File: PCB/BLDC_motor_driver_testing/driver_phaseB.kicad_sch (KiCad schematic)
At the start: 20 parts, among them Q3 IRF540N, Q4 IRF540N, U5 IR2104, U6 INA240A2D, U7 LMV393

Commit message: PCB layouting...
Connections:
- net PWR_12V: now also Q3.2 (D)
- net at C12.1, D5.1 (K), U5.8 (VB): no longer Q3.2 (D)
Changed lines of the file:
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@@
+	)
+	(junction
+		(at 66.04 93.98)
+		(diameter 0)
+		(color 0 0 0 0)
 	)
 	(junction
@@
 	)
 	(junction
+		(at 86.36 35.56)
+		(diameter 0)
+		(color 0 0 0 0)
+	)
+	(junction
 		(at 146.05 127)
 		(diameter 0)
@@
 	)
 	(junction
-		(at 83.82 64.77)
-		(diameter 0)
-		(color 0 0 0 0)
-	)
-	(junction
 		(at 129.54 120.65)
 		(diameter 0)
@@
 	(wire
 		(pts
-			(xy 113.03 64.77) (xy 113.03 69.85)
+			(xy 113.03 35.56) (xy 113.03 69.85)
 		)
 		(stroke
@@
 	(wire
 		(pts
-			(xy 66.04 92.71) (xy 66.04 96.52)
+			(xy 66.04 92.71) (xy 66.04 93.98)
 		)
 		(stroke
@@
 	(wire
 		(pts
+			(xy 55.88 93.98) (xy 66.04 93.98)
+		)
+		(stroke
+			(width 0)
+			(type default)
+		)
+	)
+	(wire
+		(pts
 			(xy 146.05 127) (xy 148.59 127)
 		)
@@
 	(wire
 		(pts
+			(xy 113.03 35.56) (xy 86.36 35.56)
+		)
+		(stroke
+			(width 0)
+			(type default)
+		)
+	)
+	(wire
+		(pts
 			(xy 99.06 74.93) (xy 101.6 74.93)
 		)
@@
 	(wire
 		(pts
-			(xy 83.82 64.77) (xy 113.03 64.77)
-		)
-		(stroke
-			(width 0)
-			(type default)
-		)
-	)
-	(wire
-		(pts
 			(xy 80.01 48.26) (xy 73.66 48.26)
 		)
@@
 		(pts
 			(xy 43.18 80.01) (xy 58.42 80.01)
+		)
+		(stroke
+			(width 0)
+			(type default)
+		)
+	)
+	(wire
+		(pts
+			(xy 66.04 93.98) (xy 66.04 96.52)
 		)
 		(stroke
@@
 		(effects
 			(font
+				(size 1.27 1.27)
+			)
+			(justify right)
+		)
+	)
+	(hierarchical_label "GND"
+		(shape input)
+		(at 55.88 93.98 180)
+		(effects
+			(font

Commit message: Test driver layout...
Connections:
- net GND_B: now reaches C14.1, Q4.3 (S), R10.1, U6.8 (+)
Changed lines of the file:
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@@
-		)
-	)
-	(label "SD_B"
-		(at 260.35 107.95 180)
-		(effects
-			(font
-				(size 1.27 1.27)
-			)
-			(justify right bottom)
 		)
 	)
@@
 		)
 	)
-	(label "SD_B"
-		(at 52.07 82.55 0)
+	(label "GND_B"
+		(at 113.03 107.95 90)
 		(effects
 			(font
@@
 		)
 	)
+	(global_label "SD_B"
+		(shape input)
+		(at 260.35 107.95 0)
+		(fields_autoplaced yes)
+		(effects
+			(font
+				(size 1.27 1.27)
+			)
+			(justify left)
+		)
+		(property "Intersheetrefs" "${INTERSHEET_REFS}"
+			(at 268.0523 107.95 0)
+			(effects
+				(font
+					(size 1.27 1.27)
+				)
+				(justify left)
+				(hide yes)
+			)
+		)
+	)

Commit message: Getting closer to finish 2 ;)
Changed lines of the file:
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@@
+	)
+	(junction
+		(at 49.53 82.55)
+		(diameter 0)
+		(color 0 0 0 0)
 	)
 	(junction
@@
 	(wire
 		(pts
-			(xy 43.18 82.55) (xy 58.42 82.55)
+			(xy 43.18 82.55) (xy 49.53 82.55)
 		)
 		(stroke
@@
 	(wire
 		(pts
+			(xy 43.18 86.36) (xy 49.53 86.36)
+		)
+		(stroke
+			(width 0)
+			(type default)
+		)
+	)
+	(wire
+		(pts
 			(xy 91.44 90.17) (xy 88.9 90.17)
 		)
@@
 	(wire
 		(pts
+			(xy 49.53 86.36) (xy 49.53 82.55)
+		)
+		(stroke
+			(width 0)
+			(type default)
+		)
+	)
+	(wire
+		(pts
 			(xy 88.9 95.25) (xy 91.44 95.25)
 		)
@@
 		(pts
 			(xy 83.82 64.77) (xy 83.82 72.39)
+		)
+		(stroke
+			(width 0)
+			(type default)
+		)
+	)
+	(wire
+		(pts
+			(xy 49.53 82.55) (xy 58.42 82.55)
 		)
 		(stroke
@@
 				(hide yes)
 			)
+		)
+	)
+	(global_label "SD_A"
+		(shape input)
+		(at 43.18 86.36 180)
+		(fields_autoplaced yes)
+		(effects
+			(font
+				(size 1.27 1.27)
+			)
+			(justify right)
+		)
+		(property "Intersheetrefs" "${INTERSHEET_REFS}"
+			(at 35.6591 86.36 0)
+			(effects
+				(font
+					(size 1.27 1.27)
+				)
+				(justify right)
+				(hide yes)
+			)

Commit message: Almost there 0_0
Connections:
- net GND: no longer R13.1, U5.3 (~{SD}), U7.1
- new net SD_B: R13.1, U5.3 (~{SD}), U7.1
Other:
- moved on the sheet: R13
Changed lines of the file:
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@@
-	)
-	(junction
-		(at 231.14 125.73)
-		(diameter 0)
-		(color 0 0 0 0)
-	)
-	(junction
-		(at 49.53 82.55)
-		(diameter 0)
-		(color 0 0 0 0)
 	)
 	(junction
@@
 	)
 	(junction
-		(at 251.46 107.95)
-		(diameter 0)
-		(color 0 0 0 0)
-	)
-	(junction
 		(at 83.82 85.09)
 		(diameter 0)
@@
 	)
 	(junction
+		(at 252.73 107.95)
+		(diameter 0)
+		(color 0 0 0 0)
+	)
+	(junction
 		(at 101.6 95.25)
 		(diameter 0)
@@
 	(wire
 		(pts
-			(xy 247.65 107.95) (xy 251.46 107.95)
-		)
-		(stroke
-			(width 0)
-			(type default)
-		)
-	)
-	(wire
-		(pts
-			(xy 43.18 82.55) (xy 49.53 82.55)
+			(xy 247.65 107.95) (xy 252.73 107.95)
 		)
 		(stroke
@@
 	(wire
 		(pts
-			(xy 251.46 107.95) (xy 251.46 125.73)
-		)
-		(stroke
-			(width 0)
-			(type default)
-		)
-	)
-	(wire
-		(pts
 			(xy 113.03 110.49) (xy 129.54 110.49)
 		)
@@
 	(wire
 		(pts
-			(xy 43.18 86.36) (xy 49.53 86.36)
-		)
-		(stroke
-			(width 0)
-			(type default)
-		)
-	)
-	(wire
-		(pts
 			(xy 91.44 90.17) (xy 88.9 90.17)
 		)
@@
 	(wire
 		(pts
-			(xy 231.14 125.73) (xy 209.55 125.73)
-		)
-		(stroke
-			(width 0)
-			(type default)
-		)
-	)
-	(wire
-		(pts
 			(xy 66.04 92.71) (xy 66.04 93.98)
 		)
@@
 	(wire
 		(pts
-			(xy 251.46 107.95) (xy 260.35 107.95)
-		)
-		(stroke
-			(width 0)
-			(type default)
-		)
-	)
-	(wire
-		(pts
 			(xy 83.82 83.82) (xy 83.82 85.09)
 		)
@@
 	(wire
 		(pts
+			(xy 252.73 107.95) (xy 262.89 107.95)
+		)
+		(stroke
+			(width 0)
+			(type default)
+		)
+	)
+	(wire
+		(pts
 			(xy 209.55 110.49) (xy 232.41 110.49)
 		)
@@
 	(wire
 		(pts
-			(xy 49.53 86.36) (xy 49.53 82.55)
-		)
-		(stroke
-			(width 0)
-			(type default)
-		)
-	)
-	(wire
-		(pts
 			(xy 88.9 95.25) (xy 91.44 95.25)
 		)
@@
 	(wire
 		(pts
-			(xy 231.14 125.73) (xy 231.14 128.27)
-		)
-		(stroke
-			(width 0)
-			(type default)
-		)
-	)
-	(wire
-		(pts
 			(xy 113.03 120.65) (xy 113.03 125.73)
 		)
@@
 	(wire
 		(pts
-			(xy 43.18 80.01) (xy 58.42 80.01)
+			(xy 49.53 80.01) (xy 58.42 80.01)
 		)
 		(stroke
@@
 	(wire
 		(pts
-			(xy 251.46 104.14) (xy 251.46 107.95)
+			(xy 252.73 104.14) (xy 252.73 107.95)
 		)
 		(stroke
@@
 	(wire
 		(pts
-			(xy 209.55 125.73) (xy 209.55 121.92)
+			(xy 209.55 127) (xy 209.55 121.92)
 		)
 		(stroke
@@
 	(wire
 		(pts
-			(xy 251.46 93.98) (xy 251.46 96.52)
+			(xy 252.73 93.98) (xy 252.73 96.52)
 		)
 		(stroke
@@
 	(wire
 		(pts
-			(xy 231.14 125.73) (xy 251.46 125.73)
-		)
-		(stroke
-			(width 0)
-			(type default)
-		)
-	)
-	(wire
-		(pts
 			(xy 101.6 95.25) (xy 105.41 95.25)
 		)
@@
 	(wire
 		(pts
-			(xy 209.55 93.98) (xy 251.46 93.98)
+			(xy 209.55 93.98) (xy 252.73 93.98)
 		)
 		(stroke
@@
 		)
 	)
+	(label "SD_B"
+		(at 262.89 107.95 180)
+		(effects
+			(font
+				(size 1.27 1.27)
+			)
+			(justify right bottom)
+		)
+	)
+	(label "SD_B"
+		(at 53.34 82.55 0)
+		(effects
+			(font
+				(size 1.27 1.27)
+			)
+			(justify left bottom)
+		)
+	)
 	(label "GND_B"
 		(at 113.03 107.95 90)
@@
 			)
 			(justify left bottom)
-		)
-	)
-	(global_label "SD_B"
-		(shape input)
-		(at 260.35 107.95 0)
-		(fields_autoplaced yes)
-		(effects
-			(font
-				(size 1.27 1.27)
-			)
-			(justify left)
-		)
-		(property "Intersheetrefs" "${INTERSHEET_REFS}"
-			(at 268.0523 107.95 0)
-			(effects
-				(font
-					(size 1.27 1.27)
-				)
-				(justify left)
-				(hide yes)
-			)
-		)
-	)
-	(global_label "SD_A"
-		(shape input)
-		(at 43.18 86.36 180)
-		(fields_autoplaced yes)
-		(effects
-			(font
-				(size 1.27 1.27)
-			)
-			(justify right)
-		)
-		(property "Intersheetrefs" "${INTERSHEET_REFS}"
-			(at 35.6591 86.36 0)
-			(effects
-				(font
-					(size 1.27 1.27)
-				)
-				(justify right)
-				(hide yes)
-			)
 		)
 	)
@@
 	(hierarchical_label "SD_B"
 		(shape input)
-		(at 43.18 82.55 180)
+		(at 49.53 82.55 180)
 		(effects
 			(font
@@
 	(hierarchical_label "PWM_IN_B"
 		(shape input)
-		(at 43.18 80.01 180)
+		(at 49.53 80.01 180)
 		(effects
 			(font
@@
 	(symbol
 		(lib_id "Device:R")
-		(at 251.46 100.33 180)
+		(at 252.73 100.33 180)
 		(unit 1)
 		(exclude_from_sim no)
@@
 		(dnp no)
 		(property "Reference" "R13"
-			(at 253.492 99.06 0)
+			(at 254.762 99.06 0)
 			(effects
 				(font
@@
 		)
 		(property "Value" "4.7K"
-			(at 253.492 101.6 0)
+			(at 254.762 101.6 0)
 			(effects
 				(font
@@
 		)
 		(property "Footprint" "Resistor_SMD:R_0805_2012Metric_Pad1.20x1.40mm_HandSolder"
-			(at 253.238 100.33 90)
+			(at 254.508 100.33 90)
 			(effects
 				(font
@@
 		)
 		(property "Datasheet" "~"
-			(at 251.46 100.33 0)
+			(at 252.73 100.33 0)
 			(effects
 				(font
@@
 		)
 		(property "Description" "Resistor"
-			(at 251.46 100.33 0)
+			(at 252.73 100.33 0)
 			(effects
 				(font
@@
 	(symbol
 		(lib_id "power:GND")
-		(at 231.14 128.27 0)
+		(at 209.55 127 0)
 		(unit 1)
 		(exclude_from_sim no)
@@
 		(dnp no)
 		(property "Reference" "#PWR025"
-			(at 231.14 134.62 0)
+			(at 209.55 133.35 0)
 			(effects
 				(font
@@
 		)
 		(property "Value" "GND"
-			(at 231.14 132.334 0)
+			(at 209.55 131.064 0)
 			(effects
 				(font
@@
 		)
 		(property "Footprint" ""
-			(at 231.14 128.27 0)
+			(at 209.55 127 0)
 			(effects
 				(font
@@
 		)
 		(property "Datasheet" ""
-			(at 231.14 128.27 0)
+			(at 209.55 127 0)
 			(effects
 				(font
@@
 		)
 		(property "Description" "Power symbol creates a global label with name \"GND\" , ground"
-			(at 231.14 128.27 0)
-			(effects
-				(font
+			(at 209.55 127 0)
+			(effects
+				(font

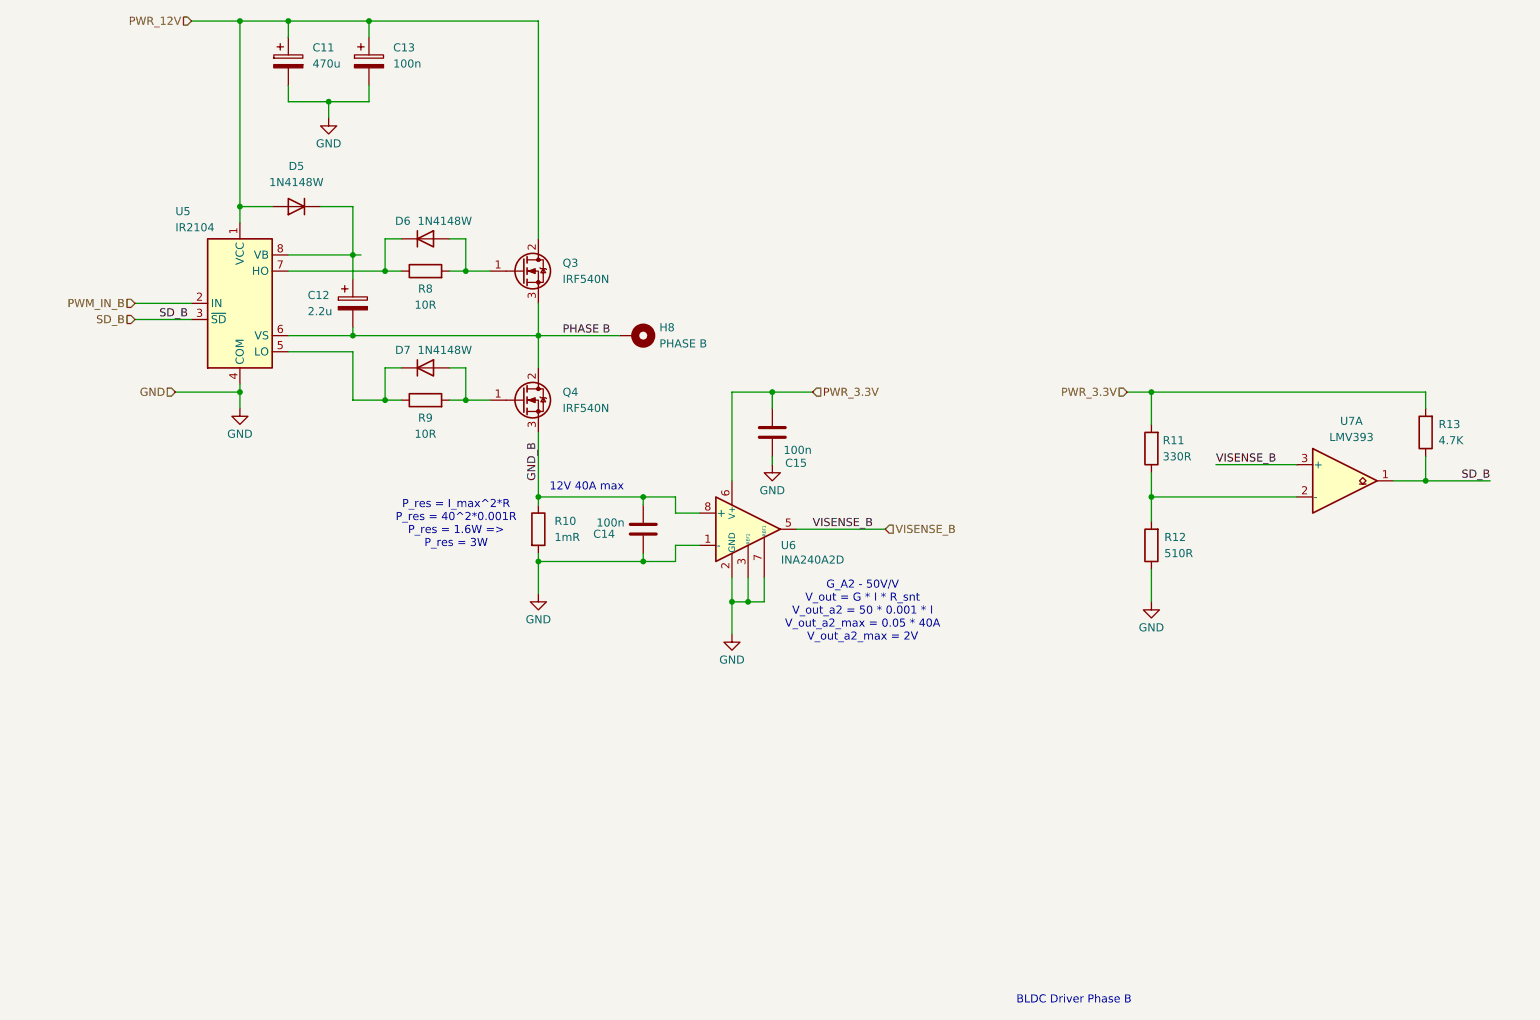
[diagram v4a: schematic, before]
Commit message: Gnd pours required, signal line EMI checking
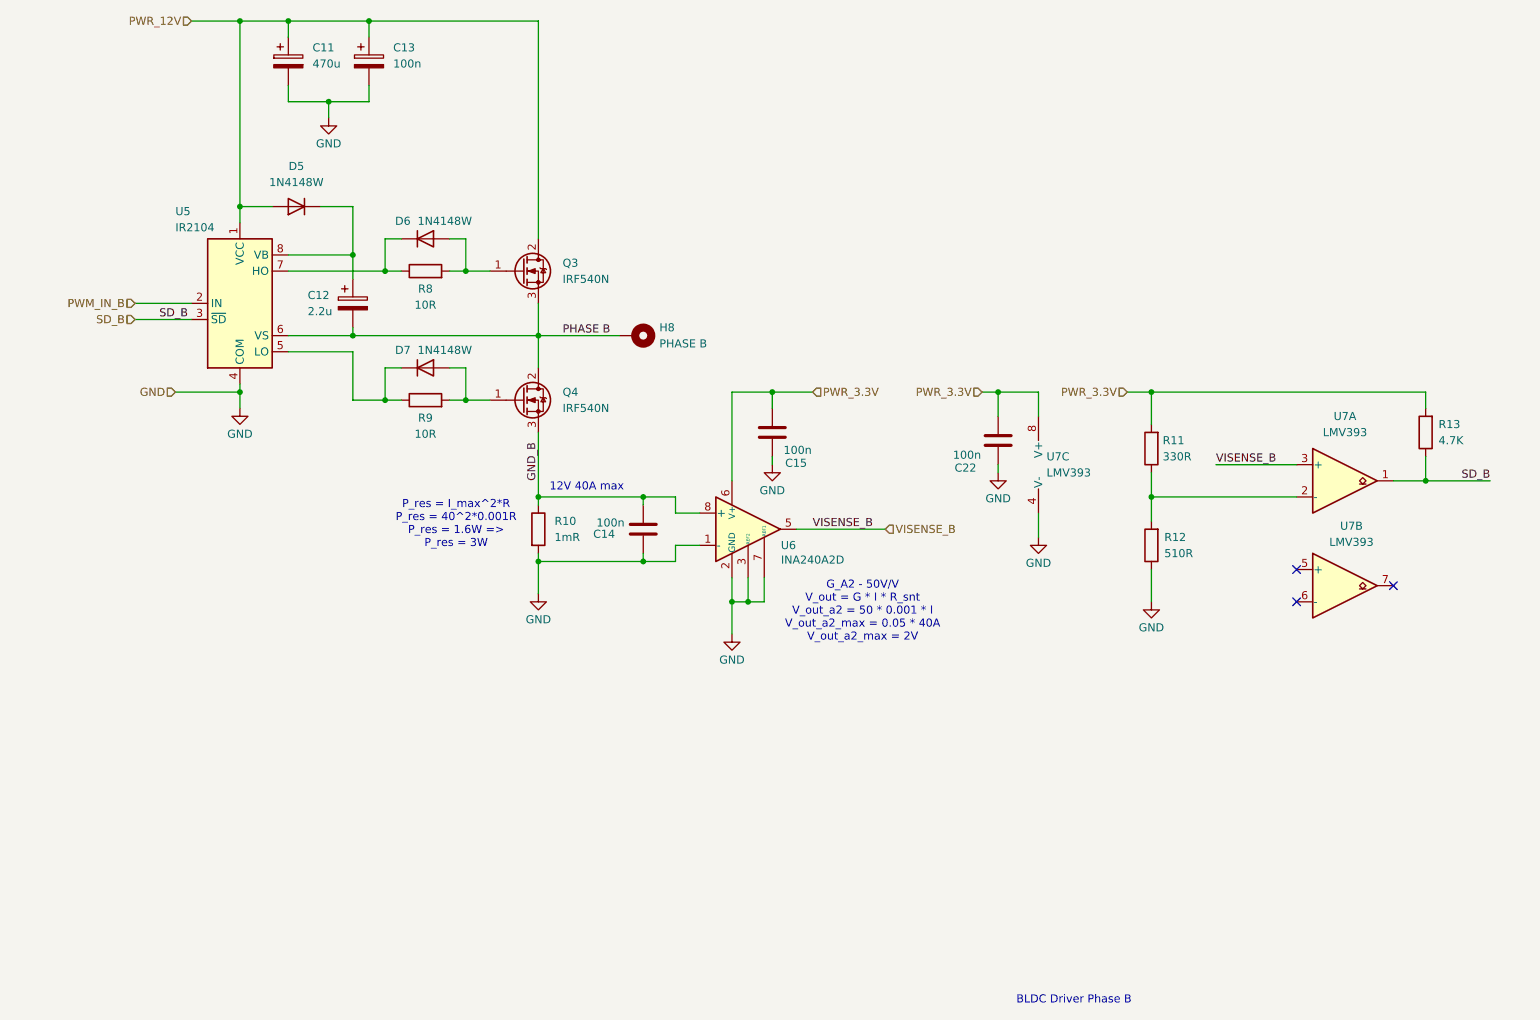
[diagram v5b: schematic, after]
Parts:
- added C22: 100n, Capacitor_SMD:C_0805_2012Metric_Pad1.18x1.45mm_HandSolder, symbol Device:C
- added unit 2 of U7
- added unit 3 of U7
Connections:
- net GND: now also C22.2, U7.4 (V-)
- net PWR_3.3V: now also C22.1, U7.8 (V+)
- no-connect marks 0 -> 3

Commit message: more changes
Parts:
- C12: value 2.2u -> 22u
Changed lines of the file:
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@@
 			)
 		)
-		(property "Value" "2.2u"
+		(property "Value" "22u"
 			(at 76.708 81.28 0)
 			(effects

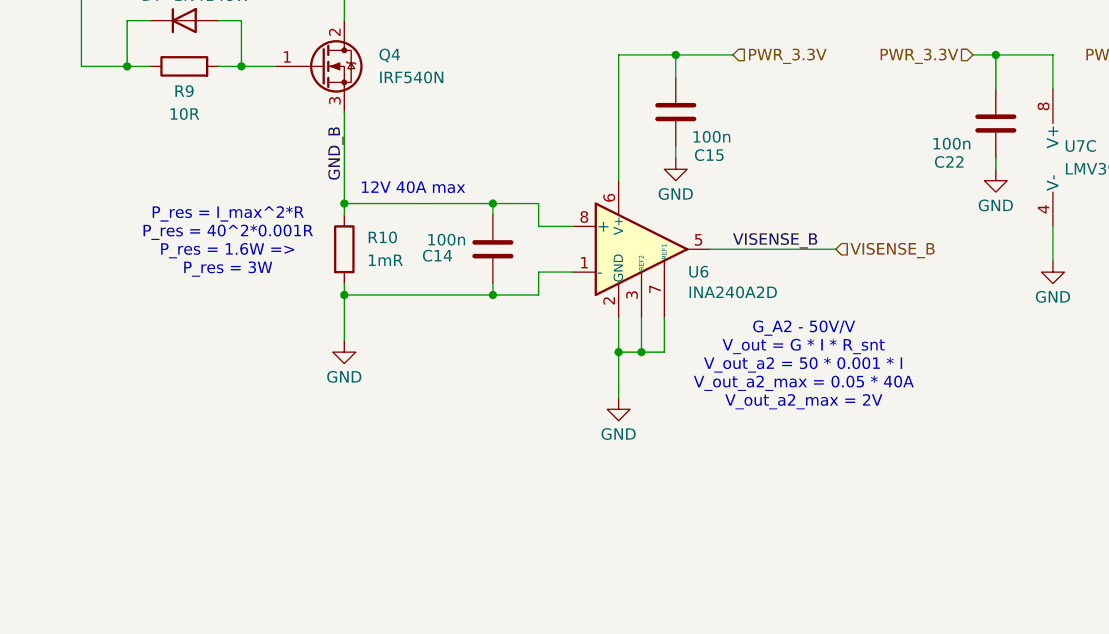
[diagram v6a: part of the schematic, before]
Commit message: small corrections for test driver
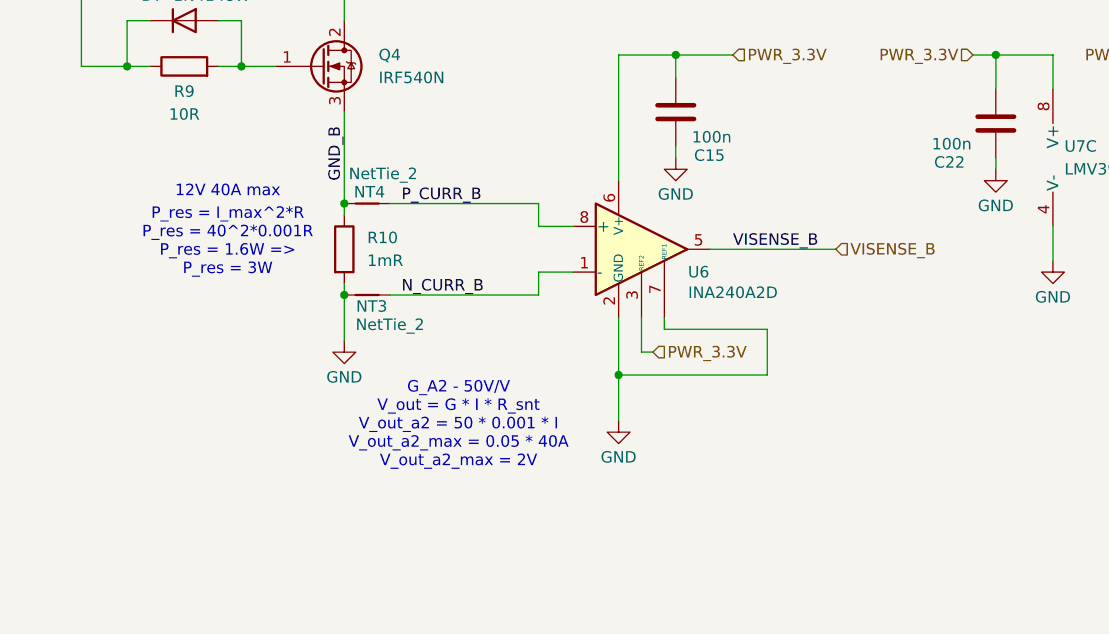
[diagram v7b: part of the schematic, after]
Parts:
- removed C14: 100n, Capacitor_SMD:C_0805_2012Metric_Pad1.18x1.45mm_HandSolder, symbol Device:C
- added NT3, NT4: NetTie_2, NetTie:NetTie-2_SMD_Pad0.5mm, symbol Device:NetTie_2
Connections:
- net GND: now also NT3.2; no longer U6.1 (-), U6.3 (REF2)
- net GND_B: now also NT4.1; no longer U6.8 (+)
- net PWR_3.3V: now also U6.3 (REF2)
- new net N_CURR_B: NT3.1, U6.1 (-)
- new net P_CURR_B: NT4.2, U6.8 (+)

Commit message: getting there...
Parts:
- R10: value 1mR -> 3mR
- R11: value 330R -> 1K
- R12: value 510R -> 10K
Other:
- note added: "12V 20A max FOC 30A max TOTAL"
- note removed: "12V 40A max"
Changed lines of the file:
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@@
 	(generator_version "9.0")
 	(paper "A4")
-	(text "12V 40A max"
+	(text "12V 20A max FOC\n	  30A max TOTAL"
 		(exclude_from_sim no)
-		(at 100.076 109.22 0)
+		(at 98.806 110.49 0)
 		(effects
 			(font
@@
 	(text "P_res = I_max^2*R\nP_res = 40^2*0.001R\nP_res = 1.6W =>\nP_res = 3W"
 		(exclude_from_sim no)
-		(at 100.076 114.808 0)
+		(at 100.076 119.38 0)
 		(effects
 			(font
@@
 			)
 		)
-		(property "Value" "330R"
+		(property "Value" "1K"
 			(at 211.328 104.14 0)
 			(effects
@@
 			)
 		)
-		(property "Value" "510R"
+		(property "Value" "10K"
 			(at 211.582 119.38 0)
 			(effects
@@
 			)
 		)
-		(property "Value" "1mR"
+		(property "Value" "3mR"
 			(at 115.57 116.8399 0)
 			(effects
